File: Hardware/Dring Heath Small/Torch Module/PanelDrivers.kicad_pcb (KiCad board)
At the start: 2 copper layers, 160 x 112.5 mm, 226 parts, among them J3 Conn_01x18_Male, J6 Motor, Q2 IRLML2402, Q3 IRLML2402, Q4 IRLML2402, Q5 IRLML2402, U1 ULN2002

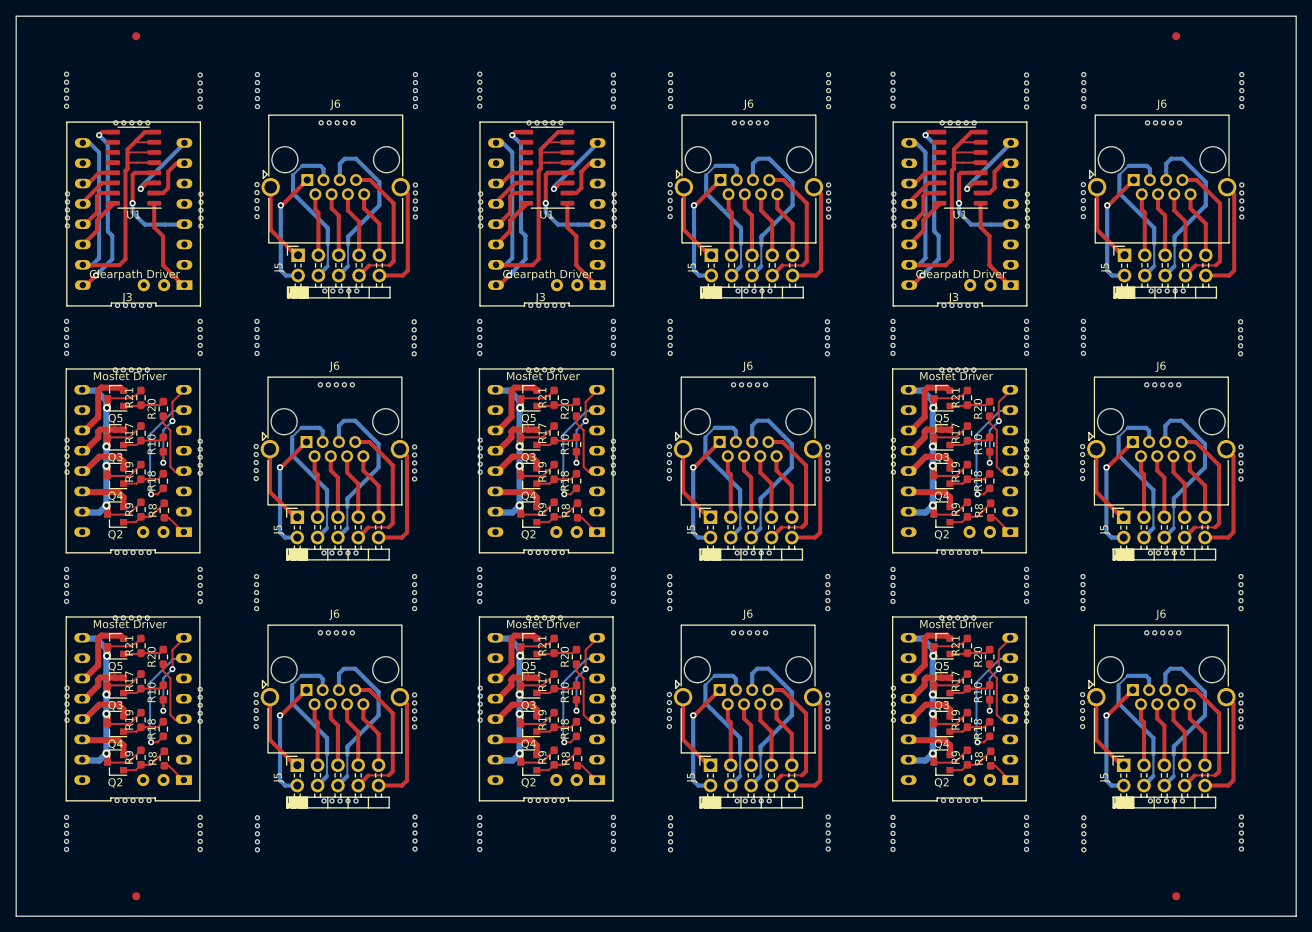
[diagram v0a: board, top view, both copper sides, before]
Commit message: Changed RJ45 conector on motor driver module
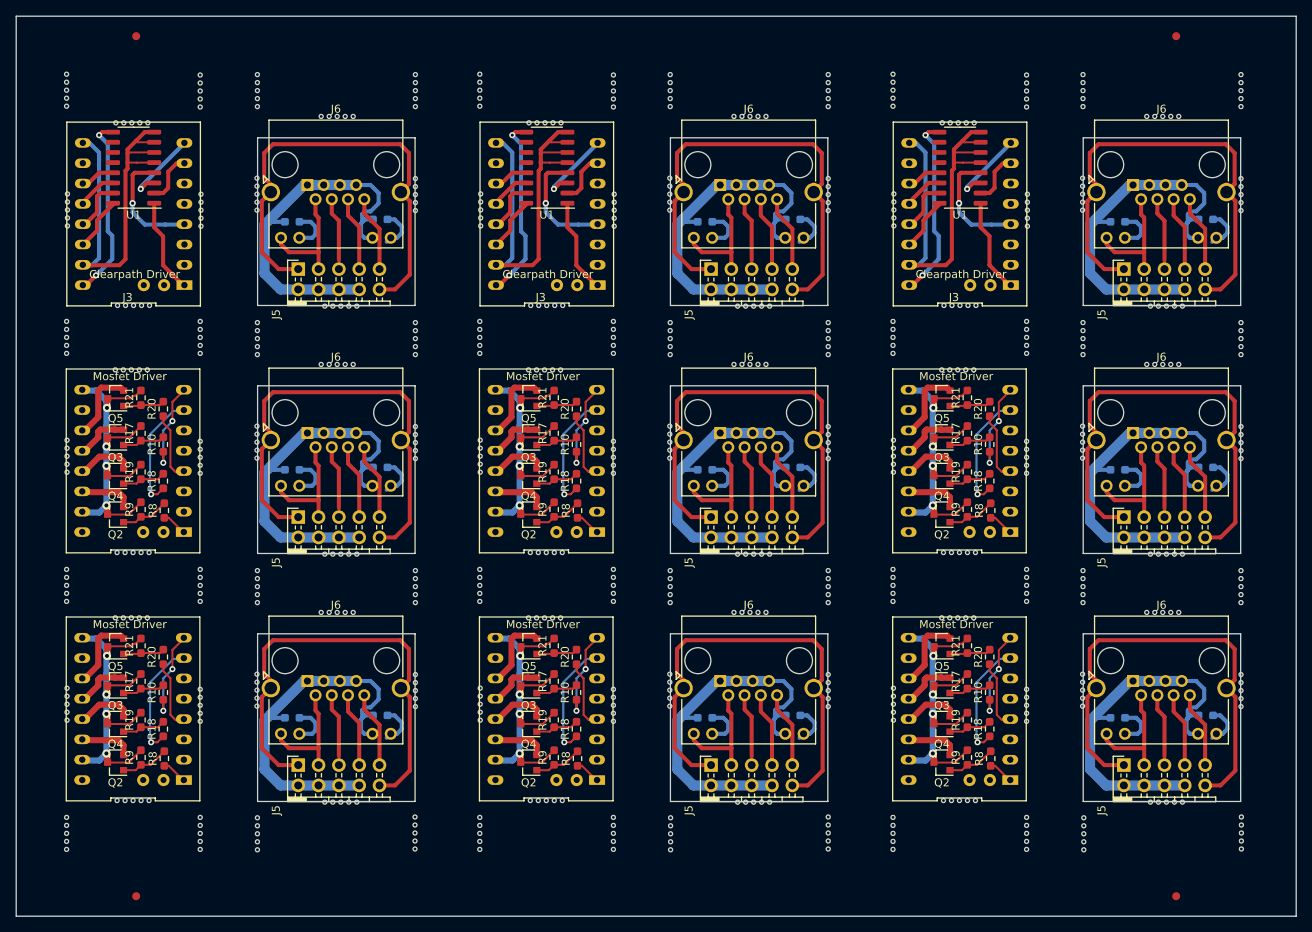
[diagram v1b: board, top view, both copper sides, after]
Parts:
- removed the J5 at (183.4, 138.6)
- removed the J5 at (131.8, 138.6)
- removed the J5 at (183.5, 74.9)
- removed the J5 at (131.9, 74.9)
- removed the J5 at (183.4, 107.6)
- removed the J5 at (131.8, 107.6)
- removed the J5 at (80.1, 138.6)
- removed the J5 at (80.1, 107.6)
- removed the J5 at (80.2, 74.9)
- removed the J6 at (184.6, 129.2)
- removed the J6 at (132.9, 129.2)
- removed the J6 at (184.6, 98.2)
- removed the J6 at (132.9, 98.2)
- removed the J6 at (184.7, 65.5)
- removed the J6 at (133.0, 65.5)
- removed the J6 at (81.3, 129.2)
- removed the J6 at (81.3, 98.2)
- removed the J6 at (81.4, 65.5)
- removed the REF** at (136.7, 121.0)
- removed the REF** at (85.0, 90.0)
- removed the REF** at (85.5, 113.1)
- removed the REF** at (95.8, 100.8)
- removed the REF** at (188.8, 144.1)
- removed the REF** at (85.1, 57.3)
- removed the REF** at (74.0, 68.0)
- removed the REF** at (96.0, 68.1)
- removed the REF** at (85.6, 80.4)
- removed the REF** at (137.1, 144.1)
- removed the REF** at (177.3, 85.2)
- removed the REF** at (125.7, 85.2)
- removed the REF** at (177.3, 117.0)
- removed the REF** at (125.7, 117.0)
- removed the REF** at (177.4, 54.3)
- removed the REF** at (125.8, 54.3)
- removed the REF** at (199.2, 131.8)
- removed the REF** at (199.2, 117.0)
- removed the REF** at (147.5, 117.0)
- removed the REF** at (199.2, 54.3)
- removed the REF** at (147.6, 54.3)
- removed the REF** at (199.1, 85.2)
- removed the REF** at (147.4, 85.2)
- removed the REF** at (199.2, 100.8)
- removed the REF** at (147.5, 100.8)
- removed the REF** at (177.2, 100.8)
- removed the REF** at (147.5, 131.8)
- removed the REF** at (125.6, 100.8)
- removed the REF** at (188.3, 90.0)
- removed the REF** at (136.7, 90.0)
- removed the REF** at (188.8, 113.1)
- removed the REF** at (137.1, 113.1)
- removed the REF** at (177.3, 68.0)
- removed the REF** at (125.7, 68.0)
- removed the REF** at (188.4, 57.3)
- removed the REF** at (136.8, 57.3)
- removed the REF** at (188.9, 80.4)
- removed the REF** at (137.2, 80.4)
- removed the REF** at (199.2, 68.1)
- removed the REF** at (147.6, 68.1)
- removed the REF** at (177.2, 131.8)
- removed the REF** at (125.6, 131.8)
- removed the REF** at (95.8, 131.8)
- removed the REF** at (74.0, 131.8)
- removed the REF** at (85.0, 121.0)
- removed the REF** at (85.5, 144.1)
- removed the REF** at (188.3, 121.0)
- removed the REF** at (95.8, 117.0)
- removed the REF** at (95.8, 85.2)
- removed the REF** at (74.0, 85.2)
- removed the REF** at (74.0, 117.0)
- removed the REF** at (74.0, 100.8)
- added J5: ~, Modules:PinSocket_2x05_Short_Horizontal, F.Cu at (183.5, 138.6)
- added J5: ~, Modules:PinSocket_2x05_Short_Horizontal, F.Cu at (131.9, 138.6)
- added J5: ~, Modules:PinSocket_2x05_Short_Horizontal, F.Cu at (80.3, 138.6)
- added J5: ~, Modules:PinSocket_2x05_Short_Horizontal, F.Cu at (183.5, 107.6)
- added J5: ~, Modules:PinSocket_2x05_Short_Horizontal, F.Cu at (131.9, 107.6)
- added J5: ~, Modules:PinSocket_2x05_Short_Horizontal, F.Cu at (80.3, 107.6)
- added J5: ~, Modules:PinSocket_2x05_Short_Horizontal, F.Cu at (183.5, 76.6)
- added J5: ~, Modules:PinSocket_2x05_Short_Horizontal, F.Cu at (131.9, 76.6)
- added J5: ~, Modules:PinSocket_2x05_Short_Horizontal, F.Cu at (80.3, 76.6)
- added J6: 8P8C_LED_Shielded, Connector_RJ:RJ45_Amphenol_RJHSE538X, F.Cu at (184.6, 128.1)
- added J6: 8P8C_LED_Shielded, Connector_RJ:RJ45_Amphenol_RJHSE538X, F.Cu at (133.0, 128.1)
- added J6: 8P8C_LED_Shielded, Connector_RJ:RJ45_Amphenol_RJHSE538X, F.Cu at (81.4, 128.1)
- added J6: 8P8C_LED_Shielded, Connector_RJ:RJ45_Amphenol_RJHSE538X, F.Cu at (184.6, 97.1)
- added J6: 8P8C_LED_Shielded, Connector_RJ:RJ45_Amphenol_RJHSE538X, F.Cu at (133.0, 97.1)
- added J6: 8P8C_LED_Shielded, Connector_RJ:RJ45_Amphenol_RJHSE538X, F.Cu at (81.4, 97.1)
- added J6: 8P8C_LED_Shielded, Connector_RJ:RJ45_Amphenol_RJHSE538X, F.Cu at (184.6, 66.1)
- added J6: 8P8C_LED_Shielded, Connector_RJ:RJ45_Amphenol_RJHSE538X, F.Cu at (133.0, 66.1)
- added J6: 8P8C_LED_Shielded, Connector_RJ:RJ45_Amphenol_RJHSE538X, F.Cu at (81.4, 66.1)
- added R40: 1k, Resistor_SMD:R_0603_1608Metric_Pad0.98x0.95mm_HandSolder, B.Cu at (193.7, 132.4)
- added R40: 1k, Resistor_SMD:R_0603_1608Metric_Pad0.98x0.95mm_HandSolder, B.Cu at (142.1, 132.4)
- added R40: 1k, Resistor_SMD:R_0603_1608Metric_Pad0.98x0.95mm_HandSolder, B.Cu at (90.5, 132.4)
- added R40: 1k, Resistor_SMD:R_0603_1608Metric_Pad0.98x0.95mm_HandSolder, B.Cu at (193.7, 101.4)
- added R40: 1k, Resistor_SMD:R_0603_1608Metric_Pad0.98x0.95mm_HandSolder, B.Cu at (142.1, 101.4)
- added R40: 1k, Resistor_SMD:R_0603_1608Metric_Pad0.98x0.95mm_HandSolder, B.Cu at (90.5, 101.4)
- added R40: 1k, Resistor_SMD:R_0603_1608Metric_Pad0.98x0.95mm_HandSolder, B.Cu at (193.7, 70.4)
- added R40: 1k, Resistor_SMD:R_0603_1608Metric_Pad0.98x0.95mm_HandSolder, B.Cu at (142.1, 70.4)
- added R40: 1k, Resistor_SMD:R_0603_1608Metric_Pad0.98x0.95mm_HandSolder, B.Cu at (90.5, 70.4)
- added R41: 1k, Resistor_SMD:R_0603_1608Metric_Pad0.98x0.95mm_HandSolder, B.Cu at (182.7, 132.7)
- added R41: 1k, Resistor_SMD:R_0603_1608Metric_Pad0.98x0.95mm_HandSolder, B.Cu at (131.1, 132.7)
- added R41: 1k, Resistor_SMD:R_0603_1608Metric_Pad0.98x0.95mm_HandSolder, B.Cu at (79.5, 132.7)
- added R41: 1k, Resistor_SMD:R_0603_1608Metric_Pad0.98x0.95mm_HandSolder, B.Cu at (182.7, 101.7)
- added R41: 1k, Resistor_SMD:R_0603_1608Metric_Pad0.98x0.95mm_HandSolder, B.Cu at (131.1, 101.7)
- added R41: 1k, Resistor_SMD:R_0603_1608Metric_Pad0.98x0.95mm_HandSolder, B.Cu at (79.5, 101.7)
- added R41: 1k, Resistor_SMD:R_0603_1608Metric_Pad0.98x0.95mm_HandSolder, B.Cu at (182.7, 70.7)
- added R41: 1k, Resistor_SMD:R_0603_1608Metric_Pad0.98x0.95mm_HandSolder, B.Cu at (131.1, 70.7)
- added R41: 1k, Resistor_SMD:R_0603_1608Metric_Pad0.98x0.95mm_HandSolder, B.Cu at (79.5, 70.7)
- added REF**: SINGLE_SIDED_TAB, Modules:SINGLE_SIDED_TAB, F.Cu at (199.2, 129.3)
- added REF**: SINGLE_SIDED_TAB, Modules:SINGLE_SIDED_TAB, F.Cu at (125.7, 129.2)
- added REF**: SINGLE_SIDED_TAB, Modules:SINGLE_SIDED_TAB, F.Cu at (74.0, 129.2)
- added REF**: SINGLE_SIDED_TAB, Modules:SINGLE_SIDED_TAB, F.Cu at (85.1, 56.5)
- added REF**: SINGLE_SIDED_TAB, Modules:SINGLE_SIDED_TAB, F.Cu at (74.0, 67.2)
- added REF**: SINGLE_SIDED_TAB, Modules:SINGLE_SIDED_TAB, F.Cu at (96.0, 67.3)
- added REF**: SINGLE_SIDED_TAB, Modules:SINGLE_SIDED_TAB, F.Cu at (85.6, 82.3)
- added REF**: SINGLE_SIDED_TAB, Modules:SINGLE_SIDED_TAB, F.Cu at (177.2, 98.2)
- added REF**: SINGLE_SIDED_TAB, Modules:SINGLE_SIDED_TAB, F.Cu at (125.7, 98.2)
- added REF**: SINGLE_SIDED_TAB, Modules:SINGLE_SIDED_TAB, F.Cu at (74.0, 98.2)
- added REF**: SINGLE_SIDED_TAB, Modules:SINGLE_SIDED_TAB, F.Cu at (177.2, 67.2)
- added REF**: SINGLE_SIDED_TAB, Modules:SINGLE_SIDED_TAB, F.Cu at (125.7, 67.2)
- added REF**: SINGLE_SIDED_TAB, Modules:SINGLE_SIDED_TAB, F.Cu at (177.3, 116.3)
- added REF**: SINGLE_SIDED_TAB, Modules:SINGLE_SIDED_TAB, F.Cu at (125.7, 116.3)
- added REF**: SINGLE_SIDED_TAB, Modules:SINGLE_SIDED_TAB, F.Cu at (74.1, 116.3)
- added REF**: SINGLE_SIDED_TAB, Modules:SINGLE_SIDED_TAB, F.Cu at (147.6, 129.3)
- added REF**: SINGLE_SIDED_TAB, Modules:SINGLE_SIDED_TAB, F.Cu at (177.3, 85.3)
- added REF**: SINGLE_SIDED_TAB, Modules:SINGLE_SIDED_TAB, F.Cu at (125.7, 85.3)
- added REF**: SINGLE_SIDED_TAB, Modules:SINGLE_SIDED_TAB, F.Cu at (74.1, 85.3)
- added REF**: SINGLE_SIDED_TAB, Modules:SINGLE_SIDED_TAB, F.Cu at (177.3, 54.3)
- added REF**: SINGLE_SIDED_TAB, Modules:SINGLE_SIDED_TAB, F.Cu at (125.7, 54.3)
- added REF**: SINGLE_SIDED_TAB, Modules:SINGLE_SIDED_TAB, F.Cu at (188.8, 144.3)
- added REF**: SINGLE_SIDED_TAB, Modules:SINGLE_SIDED_TAB, F.Cu at (137.2, 144.3)
- added REF**: SINGLE_SIDED_TAB, Modules:SINGLE_SIDED_TAB, F.Cu at (85.6, 144.3)
- added REF**: SINGLE_SIDED_TAB, Modules:SINGLE_SIDED_TAB, F.Cu at (188.8, 113.3)
- added REF**: SINGLE_SIDED_TAB, Modules:SINGLE_SIDED_TAB, F.Cu at (137.2, 113.3)
- added REF**: SINGLE_SIDED_TAB, Modules:SINGLE_SIDED_TAB, F.Cu at (96.0, 129.3)
- added REF**: SINGLE_SIDED_TAB, Modules:SINGLE_SIDED_TAB, F.Cu at (85.6, 113.3)
- added REF**: SINGLE_SIDED_TAB, Modules:SINGLE_SIDED_TAB, F.Cu at (188.8, 82.3)
- added REF**: SINGLE_SIDED_TAB, Modules:SINGLE_SIDED_TAB, F.Cu at (137.2, 82.3)
- added REF**: SINGLE_SIDED_TAB, Modules:SINGLE_SIDED_TAB, F.Cu at (199.2, 116.3)
- added REF**: SINGLE_SIDED_TAB, Modules:SINGLE_SIDED_TAB, F.Cu at (147.6, 116.3)
- added REF**: SINGLE_SIDED_TAB, Modules:SINGLE_SIDED_TAB, F.Cu at (96.0, 116.3)
- added REF**: SINGLE_SIDED_TAB, Modules:SINGLE_SIDED_TAB, F.Cu at (199.2, 85.3)
- added REF**: SINGLE_SIDED_TAB, Modules:SINGLE_SIDED_TAB, F.Cu at (147.6, 85.3)
- added REF**: SINGLE_SIDED_TAB, Modules:SINGLE_SIDED_TAB, F.Cu at (96.0, 85.3)
- added REF**: SINGLE_SIDED_TAB, Modules:SINGLE_SIDED_TAB, F.Cu at (199.2, 54.3)
- added REF**: SINGLE_SIDED_TAB, Modules:SINGLE_SIDED_TAB, F.Cu at (199.2, 98.3)
- added REF**: SINGLE_SIDED_TAB, Modules:SINGLE_SIDED_TAB, F.Cu at (147.6, 54.3)
- added REF**: SINGLE_SIDED_TAB, Modules:SINGLE_SIDED_TAB, F.Cu at (188.3, 118.5)
- added REF**: SINGLE_SIDED_TAB, Modules:SINGLE_SIDED_TAB, F.Cu at (136.7, 118.5)
- added REF**: SINGLE_SIDED_TAB, Modules:SINGLE_SIDED_TAB, F.Cu at (85.1, 118.5)
- added REF**: SINGLE_SIDED_TAB, Modules:SINGLE_SIDED_TAB, F.Cu at (188.3, 87.5)
- added REF**: SINGLE_SIDED_TAB, Modules:SINGLE_SIDED_TAB, F.Cu at (136.7, 87.5)
- added REF**: SINGLE_SIDED_TAB, Modules:SINGLE_SIDED_TAB, F.Cu at (85.1, 87.5)
- added REF**: SINGLE_SIDED_TAB, Modules:SINGLE_SIDED_TAB, F.Cu at (188.3, 56.5)
- added REF**: SINGLE_SIDED_TAB, Modules:SINGLE_SIDED_TAB, F.Cu at (136.7, 56.5)
- added REF**: SINGLE_SIDED_TAB, Modules:SINGLE_SIDED_TAB, F.Cu at (147.6, 98.3)
- added REF**: SINGLE_SIDED_TAB, Modules:SINGLE_SIDED_TAB, F.Cu at (96.0, 98.3)
- added REF**: SINGLE_SIDED_TAB, Modules:SINGLE_SIDED_TAB, F.Cu at (199.2, 67.3)
- added REF**: SINGLE_SIDED_TAB, Modules:SINGLE_SIDED_TAB, F.Cu at (147.6, 67.3)
- added REF**: SINGLE_SIDED_TAB, Modules:SINGLE_SIDED_TAB, F.Cu at (177.2, 129.2)
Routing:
- net Net-(J5-Pad1): track 90.7 -> 535.7 mm
- net Net-(J5-Pad2): track 136.5 -> 423.3 mm, vias 9 -> 0
- net Net-(J5-Pad6): track 211.6 -> 0.00 mm
- net Net-(J5-Pad4): track 202.3 -> 0.00 mm
- net Net-(J5-Pad8): track 167.3 -> 0.00 mm
- net Net-(J5-Pad10): track 131.4 -> 0.00 mm
- net Net-(J5-Pad3): track 74.6 -> 133.1 mm
- net Net-(J6-Pad12): track 0.00 -> 52.9 mm
- net Net-(J6-Pad10): track 0.00 -> 49.0 mm
- net Net-(J5-Pad7): track 76.4 -> 86.3 mm
- net Net-(J5-Pad9): track 81.3 -> 85.6 mm
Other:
- outline, holes or cut-outs redrawn
